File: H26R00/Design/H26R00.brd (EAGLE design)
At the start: 34.6 x 30 mm, 37 parts, among them P1 HEXABIT_17.32_NO_P6_P7_P12, P2 CON-PHOENIX-350_1751277, P3 CON-PHOENIX-350_1751248, U2 HX711, X1 XTALL_CSTCE8M00G52

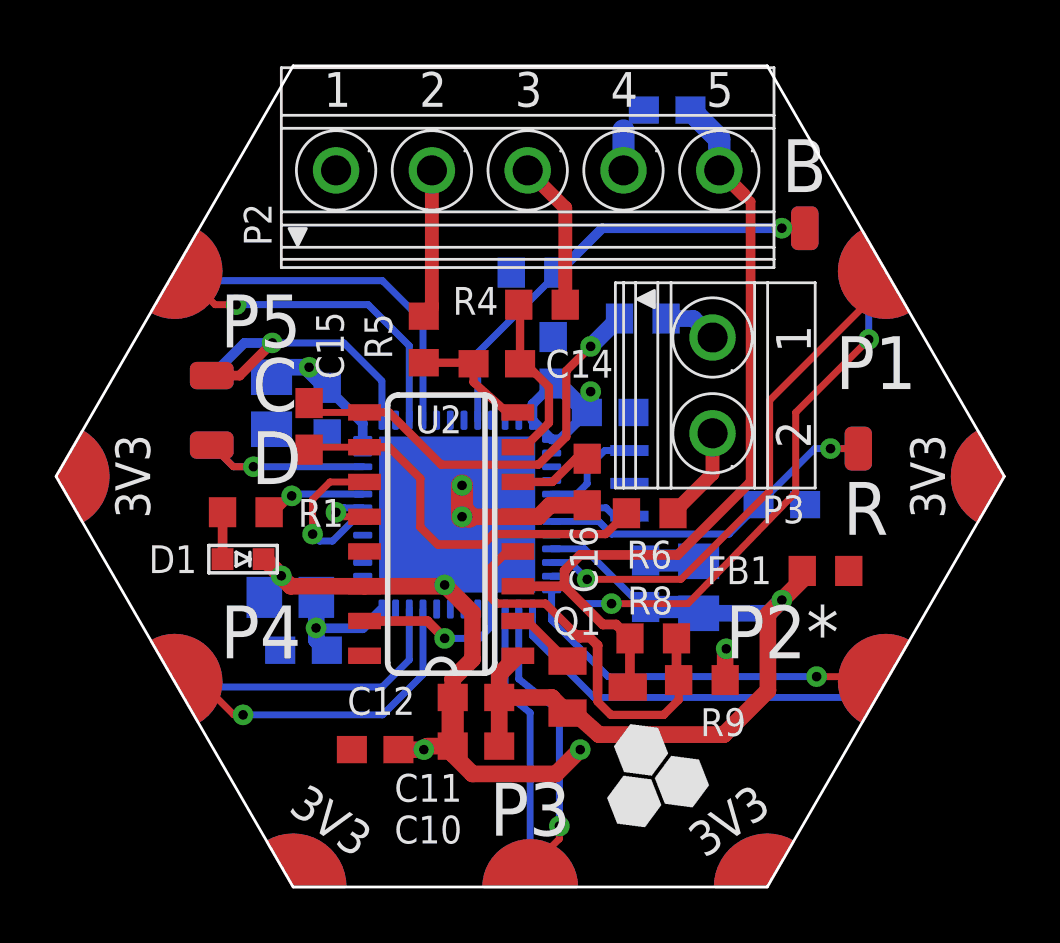
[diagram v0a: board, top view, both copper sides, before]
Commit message: Adding 3.3V to 5V converter to power the bridge Power the HX711 and bridge from 5V and don't use HX711 regulator
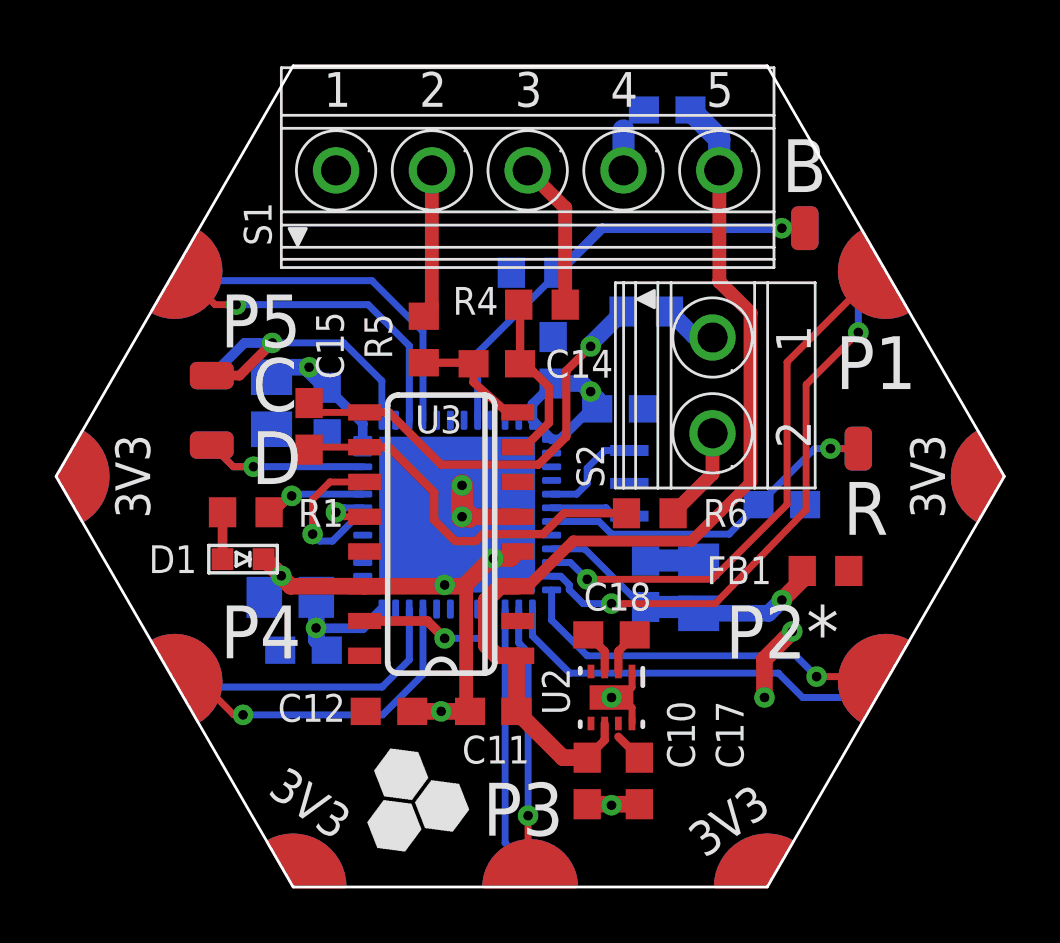
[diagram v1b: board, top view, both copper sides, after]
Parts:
- removed C16: 100nF, Hexabitz:C-0603
- removed Q1: (no value), Hexabitz:SEMICON-SMD-IPC_SOT23
- removed R8, R9: 10K, Hexabitz:R-0603
- added C17: 10uF, Hexabitz:C-0603
- added C18: 1uF, Hexabitz:C-0603
- added U3: HX711, Hexabitz:HX711_SO16
- D1: value VLMS1300-GS08 -> RED
- U2: value HX711 -> LM2775-Q1; device Hexabitz:HX711_SO16 -> Hexabitz:DSG0008A
- moved U2 8.62 mm to (37.6, 26.5), turned to 270 degrees
- moved C10 4.26 mm to (36.7, 23.5), turned to 270 degrees
- moved C12 1.49 mm to (29.5, 26.0)
- moved C11 0.81 mm to (33.3, 26.0)
- moved C9 0.40 mm to (37.9, 37.1)
- moved R7 0.28 mm to (38.9, 40.6)
- renumbered P2 to S1, P3 to S2
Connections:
- removed net N$1: C13.1, Q1.3, R8.2, S1.5, U2.3
- removed net N$10: C16.2, U2.6
- removed net N$11: R8.1, R9.2, U2.4
- removed net N$8: Q1.1, U2.2
- new net +5V: C10.1, C11.1, C13.1, S1.5, U2.6, U3.1, U3.3
- new net N$13: C18.2, U2.2
- new net N$3: C18.1, U2.3
- net DOUT: now also U3.12; no longer U2.12
- net GND: now also C17.2, U2.1, U2.8, U2.9, U3.14, U3.4, U3.5; no longer C16.1, R9.1, U2.14, U2.5
- net INA+: now also U3.8; no longer U2.8
- net INA-: now also U3.7; no longer U2.7
- net INB+: now also U3.10; no longer U2.10
- net INB-: now also U3.9; no longer U2.9
- net RATE: now also U3.15; no longer U2.15
- net SCK: now also U3.11; no longer U2.11
- net VDD: now also C17.1, U2.4, U2.5, U2.7, U3.16; no longer U2.16
- net VDDA: no longer C10.1, C11.1, Q1.2, U2.1
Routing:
- net +5V: track 0.00 -> 35.7 mm
- net N$1: track 30.3 -> 0.00 mm
- net VDDA: track 29.6 -> 11.0 mm
- net N$11: track 15.1 -> 0.00 mm
- net N$10: track 2.89 -> 0.00 mm
- net N$8: track 2.42 -> 0.00 mm
- net VDD: track 16.6 -> 18.6 mm
- net N$13: track 0.00 -> 1.58 mm
- net N$3: track 0.00 -> 1.58 mm
- net USART6_TX: track 10.6 -> 9.64 mm
- net USART4_TX: track 18.7 -> 19.4 mm
- net GND: track 32.0 -> 31.4 mm, vias 7 -> 10
- net USART4_RX: track 20.0 -> 20.6 mm
- net INB+: track 14.6 -> 14.1 mm
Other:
- board text added: "GND"
